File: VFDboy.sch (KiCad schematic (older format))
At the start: 44 parts, among them J1 AVR-ISP-6, SW1 RIGHT, SW2 A, SW3 DOWN, SW4 UP, SW5 LEFT, SW6 B, U1 ATmega32U4-MU, U2 SSD1306_VFD, U7 SRV05-4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

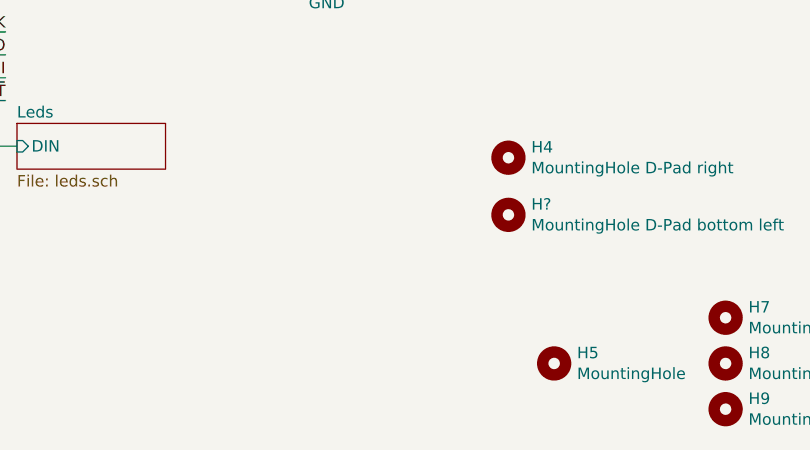
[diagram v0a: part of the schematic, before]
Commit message: Add Game Boy compatible D-Pad mounting holes
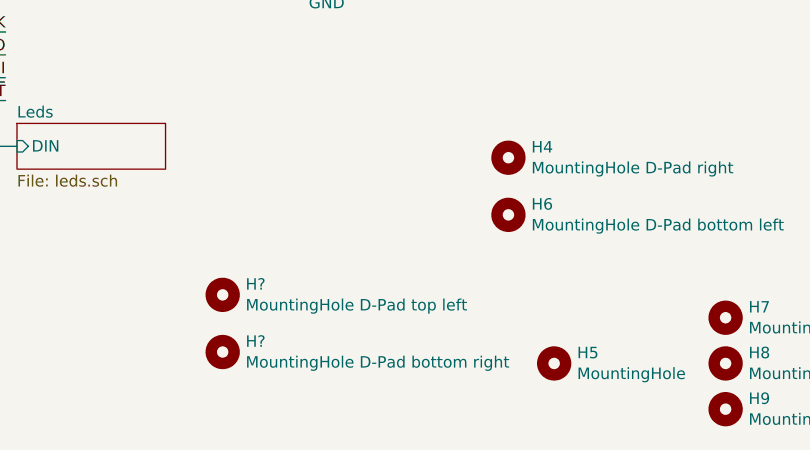
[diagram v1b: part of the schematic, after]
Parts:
- added H?: MountingHole D-Pad top left, MountingHole_GameBoy:MountingHole_GameBoy_DPAD, symbol Mechanical:MountingHole
- added H?: MountingHole D-Pad bottom right, MountingHole_GameBoy:MountingHole_GameBoy_DPAD, symbol Mechanical:MountingHole
- gave numbers to parts that had none: 1
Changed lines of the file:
@@
 $EndComp
 $Comp
-L Mechanical:MountingHole H?
+L Mechanical:MountingHole H6
 U 1 1 620E34B6
 P 4350 6700
-F 0 "H?" H 4450 6746 50  0000 L CNN
+F 0 "H6" H 4450 6746 50  0000 L CNN
 F 1 "MountingHole D-Pad bottom left" H 4450 6655 50  0000 L CNN
 F 2 "MountingHole_GBA:MountingHole_GBA_DPAD" H 4350 6700 50  0001 C CNN
@@
 	1    0    0    -1
 $EndComp
+$Comp
+L Mechanical:MountingHole H?
+U 1 1 620F5804
+P 3100 7050
+F 0 "H?" H 3200 7096 50  0000 L CNN
+F 1 "MountingHole D-Pad top left" H 3200 7005 50  0000 L CNN
+F 2 "MountingHole_GameBoy:MountingHole_GameBoy_DPAD" H 3100 7050 50  0001 C CNN
+F 3 "~" H 3100 7050 50  0001 C CNN
+	1    3100 7050
+	1    0    0    -1
+$EndComp
+$Comp
+L Mechanical:MountingHole H?
+U 1 1 621007C1
+P 3100 7300
+F 0 "H?" H 3200 7346 50  0000 L CNN
+F 1 "MountingHole D-Pad bottom right" H 3200 7255 50  0000 L CNN
+F 2 "MountingHole_GameBoy:MountingHole_GameBoy_DPAD" H 3100 7300 50  0001 C CNN
+F 3 "~" H 3100 7300 50  0001 C CNN
+	1    3100 7300
+	1    0    0    -1
+$EndComp

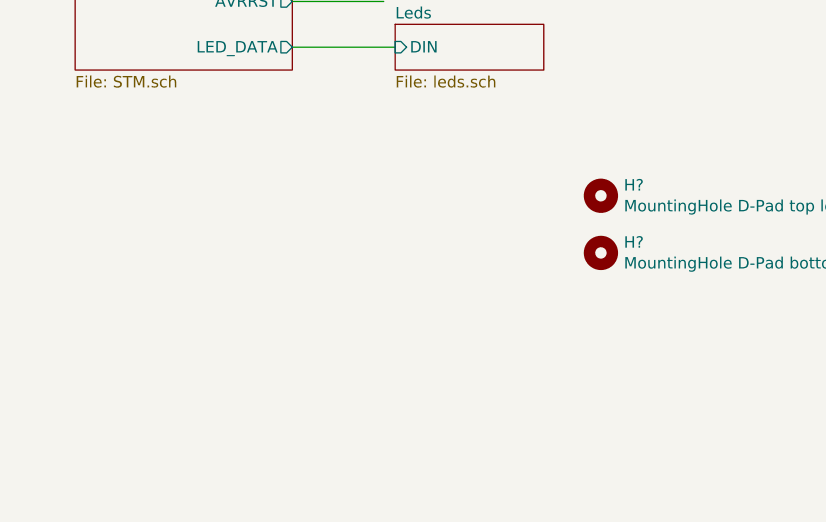
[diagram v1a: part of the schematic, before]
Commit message: Add AB button mounting
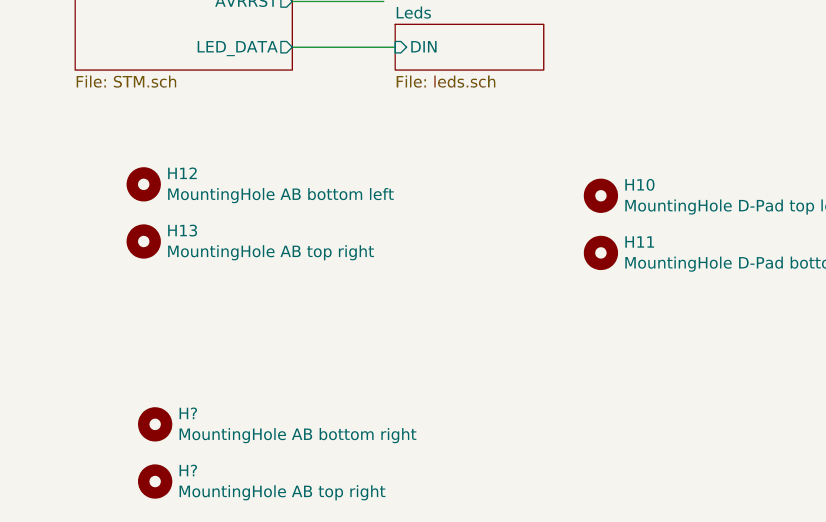
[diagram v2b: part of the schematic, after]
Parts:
- added H12: MountingHole AB bottom left, MountingHole_GameBoy:MountingHole_GameBoy_DPAD, symbol Mechanical:MountingHole
- added H13, H?: MountingHole AB top right, MountingHole_GameBoy:MountingHole_GameBoy_DPAD, symbol Mechanical:MountingHole
- added H?: MountingHole AB bottom right, MountingHole_GBA:MountingHole_GBA_AB_bottom_right, symbol Mechanical:MountingHole
- gave numbers to parts that had none: 2
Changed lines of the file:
@@
 $EndComp
 $Comp
-L Mechanical:MountingHole H?
+L Mechanical:MountingHole H10
 U 1 1 620F5804
 P 3100 7050
-F 0 "H?" H 3200 7096 50  0000 L CNN
+F 0 "H10" H 3200 7096 50  0000 L CNN
 F 1 "MountingHole D-Pad top left" H 3200 7005 50  0000 L CNN
 F 2 "MountingHole_GameBoy:MountingHole_GameBoy_DPAD" H 3100 7050 50  0001 C CNN
@@
 $EndComp
 $Comp
-L Mechanical:MountingHole H?
+L Mechanical:MountingHole H11
 U 1 1 621007C1
 P 3100 7300
-F 0 "H?" H 3200 7346 50  0000 L CNN
+F 0 "H11" H 3200 7346 50  0000 L CNN
 F 1 "MountingHole D-Pad bottom right" H 3200 7255 50  0000 L CNN
 F 2 "MountingHole_GameBoy:MountingHole_GameBoy_DPAD" H 3100 7300 50  0001 C CNN
@@
 	1    0    0    -1
 $EndComp
+$Comp
+L Mechanical:MountingHole H12
+U 1 1 6212859B
+P 1100 7000
+F 0 "H12" H 1200 7046 50  0000 L CNN
+F 1 "MountingHole AB bottom left" H 1200 6955 50  0000 L CNN
+F 2 "MountingHole_GameBoy:MountingHole_GameBoy_DPAD" H 1100 7000 50  0001 C CNN
+F 3 "~" H 1100 7000 50  0001 C CNN
+	1    1100 7000
+	1    0    0    -1
+$EndComp
+$Comp
+L Mechanical:MountingHole H13
+U 1 1 621285A1
+P 1100 7250
+F 0 "H13" H 1200 7296 50  0000 L CNN
+F 1 "MountingHole AB top right" H 1200 7205 50  0000 L CNN
+F 2 "MountingHole_GameBoy:MountingHole_GameBoy_DPAD" H 1100 7250 50  0001 C CNN
+F 3 "~" H 1100 7250 50  0001 C CNN
+	1    1100 7250
+	1    0    0    -1
+$EndComp
+$Comp
+L Mechanical:MountingHole H?
+U 1 1 6213C8C1
+P 1150 8050
+F 0 "H?" H 1250 8096 50  0000 L CNN
+F 1 "MountingHole AB bottom right" H 1250 8005 50  0000 L CNN
+F 2 "MountingHole_GBA:MountingHole_GBA_AB_bottom_right" H 1150 8050 50  0001 C CNN
+F 3 "~" H 1150 8050 50  0001 C CNN
+	1    1150 8050
+	1    0    0    -1
+$EndComp
+$Comp
+L Mechanical:MountingHole H?
+U 1 1 6213C8C7
+P 1150 8300
+F 0 "H?" H 1250 8346 50  0000 L CNN
+F 1 "MountingHole AB top right" H 1250 8255 50  0000 L CNN
+F 2 "MountingHole_GameBoy:MountingHole_GameBoy_DPAD" H 1150 8300 50  0001 C CNN
+F 3 "~" H 1150 8300 50  0001 C CNN
+	1    1150 8300
+	1    0    0    -1
+$EndComp

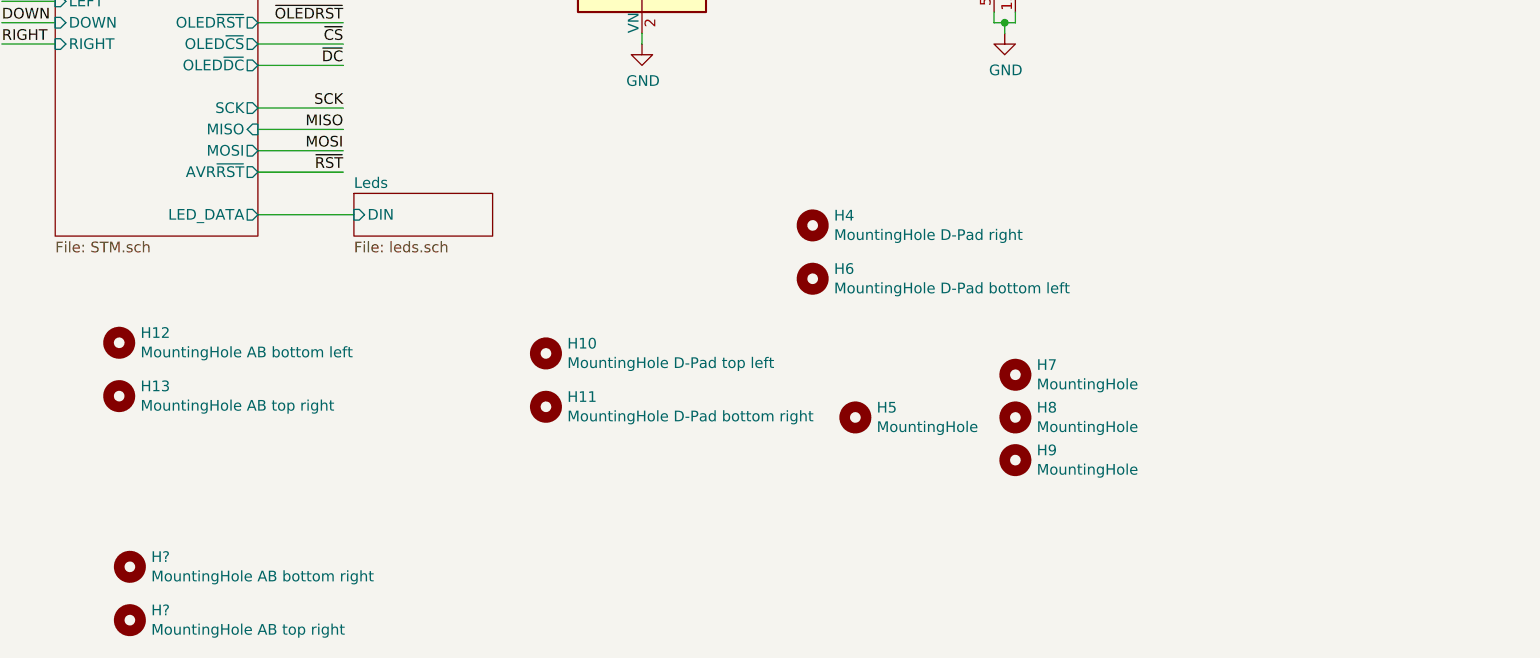
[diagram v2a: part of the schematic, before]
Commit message: Add tooling holes
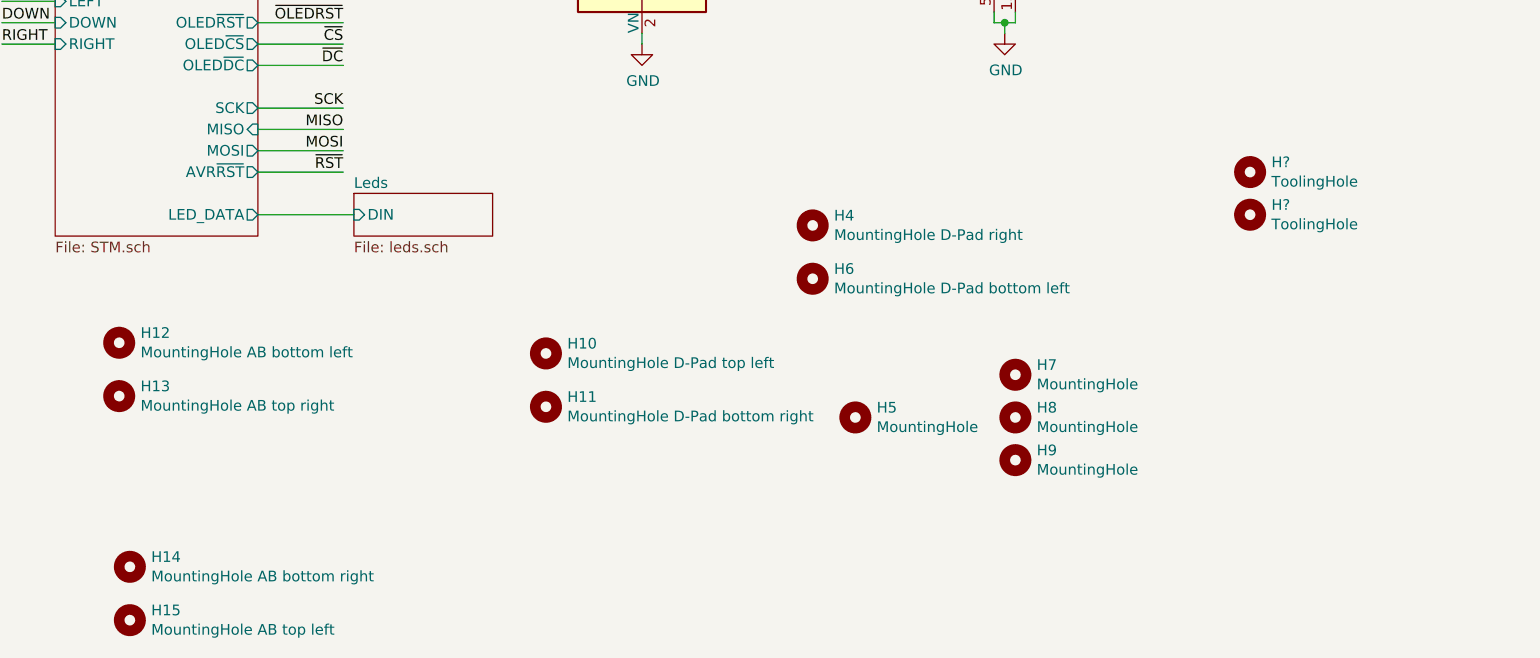
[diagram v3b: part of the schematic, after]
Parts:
- added H? (x2): ToolingHole, ToolingHole:ToolingHole_JLCSMT, symbol Mechanical:MountingHole
- H15: renamed from H?; value MountingHole AB top right -> MountingHole AB top left; footprint MountingHole_GameBoy:MountingHole_GameBoy_DPAD -> MountingHole:MountingHole_3.5mm
- gave numbers to parts that had none: 1
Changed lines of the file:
@@
 $EndComp
 $Comp
-L Mechanical:MountingHole H?
+L Mechanical:MountingHole H14
 U 1 1 6213C8C1
 P 1150 8050
-F 0 "H?" H 1250 8096 50  0000 L CNN
+F 0 "H14" H 1250 8096 50  0000 L CNN
 F 1 "MountingHole AB bottom right" H 1250 8005 50  0000 L CNN
 F 2 "MountingHole_GBA:MountingHole_GBA_AB_bottom_right" H 1150 8050 50  0001 C CNN
@@
 $EndComp
 $Comp
-L Mechanical:MountingHole H?
+L Mechanical:MountingHole H15
 U 1 1 6213C8C7
 P 1150 8300
-F 0 "H?" H 1250 8346 50  0000 L CNN
-F 1 "MountingHole AB top right" H 1250 8255 50  0000 L CNN
-F 2 "MountingHole_GameBoy:MountingHole_GameBoy_DPAD" H 1150 8300 50  0001 C CNN
+F 0 "H15" H 1250 8346 50  0000 L CNN
+F 1 "MountingHole AB top left" H 1250 8255 50  0000 L CNN
+F 2 "MountingHole:MountingHole_3.5mm" H 1150 8300 50  0001 C CNN
 F 3 "~" H 1150 8300 50  0001 C CNN
 	1    1150 8300
 	1    0    0    -1
 $EndComp
+$Comp
+L Mechanical:MountingHole H?
+U 1 1 621E7530
+P 6400 6200
+F 0 "H?" H 6500 6246 50  0000 L CNN
+F 1 "ToolingHole" H 6500 6155 50  0000 L CNN
+F 2 "ToolingHole:ToolingHole_JLCSMT" H 6400 6200 50  0001 C CNN
+F 3 "~" H 6400 6200 50  0001 C CNN
+	1    6400 6200
+	1    0    0    -1
+$EndComp
+$Comp
+L Mechanical:MountingHole H?
+U 1 1 621E8454
+P 6400 6400
+F 0 "H?" H 6500 6446 50  0000 L CNN
+F 1 "ToolingHole" H 6500 6355 50  0000 L CNN
+F 2 "ToolingHole:ToolingHole_JLCSMT" H 6400 6400 50  0001 C CNN
+F 3 "~" H 6400 6400 50  0001 C CNN
+	1    6400 6400
+	1    0    0    -1
+$EndComp

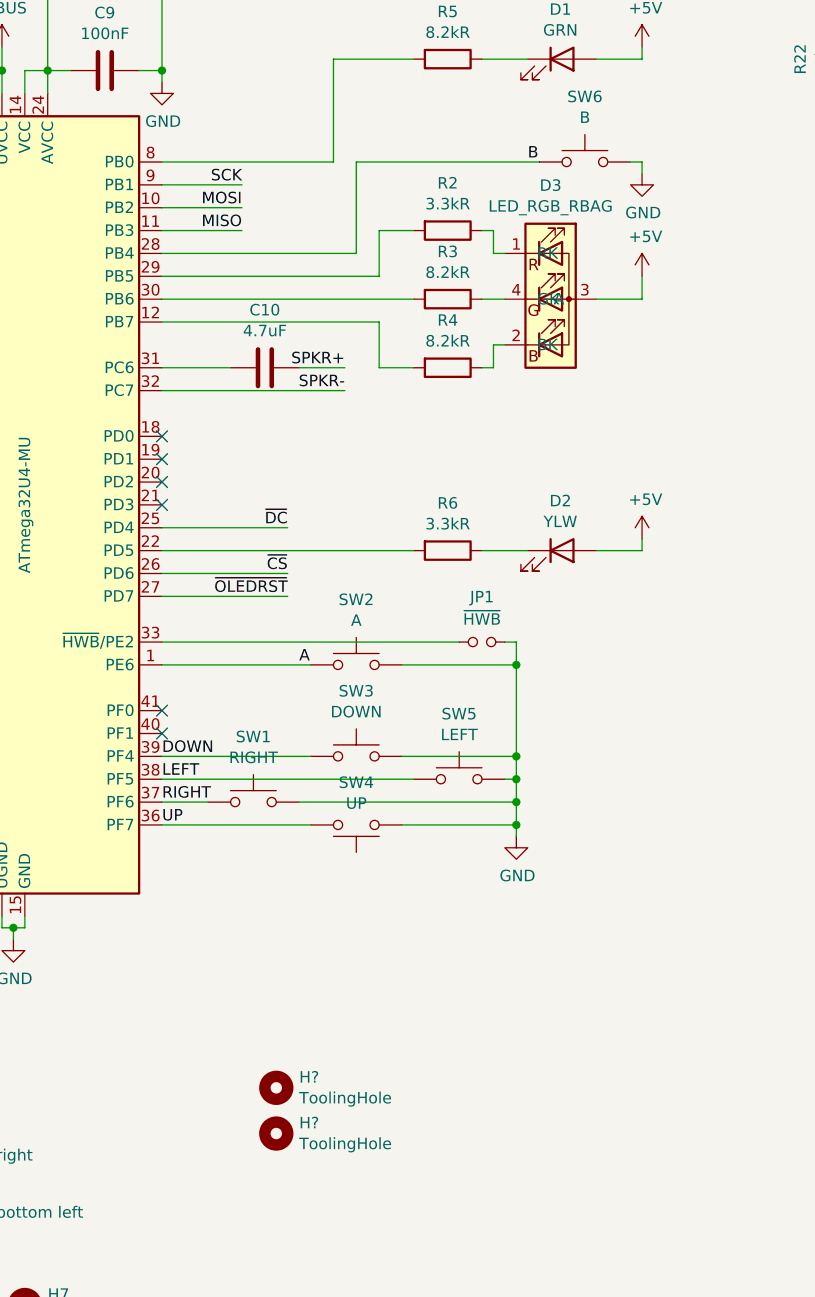
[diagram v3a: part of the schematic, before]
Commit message: Place and route WS2812 LEDs
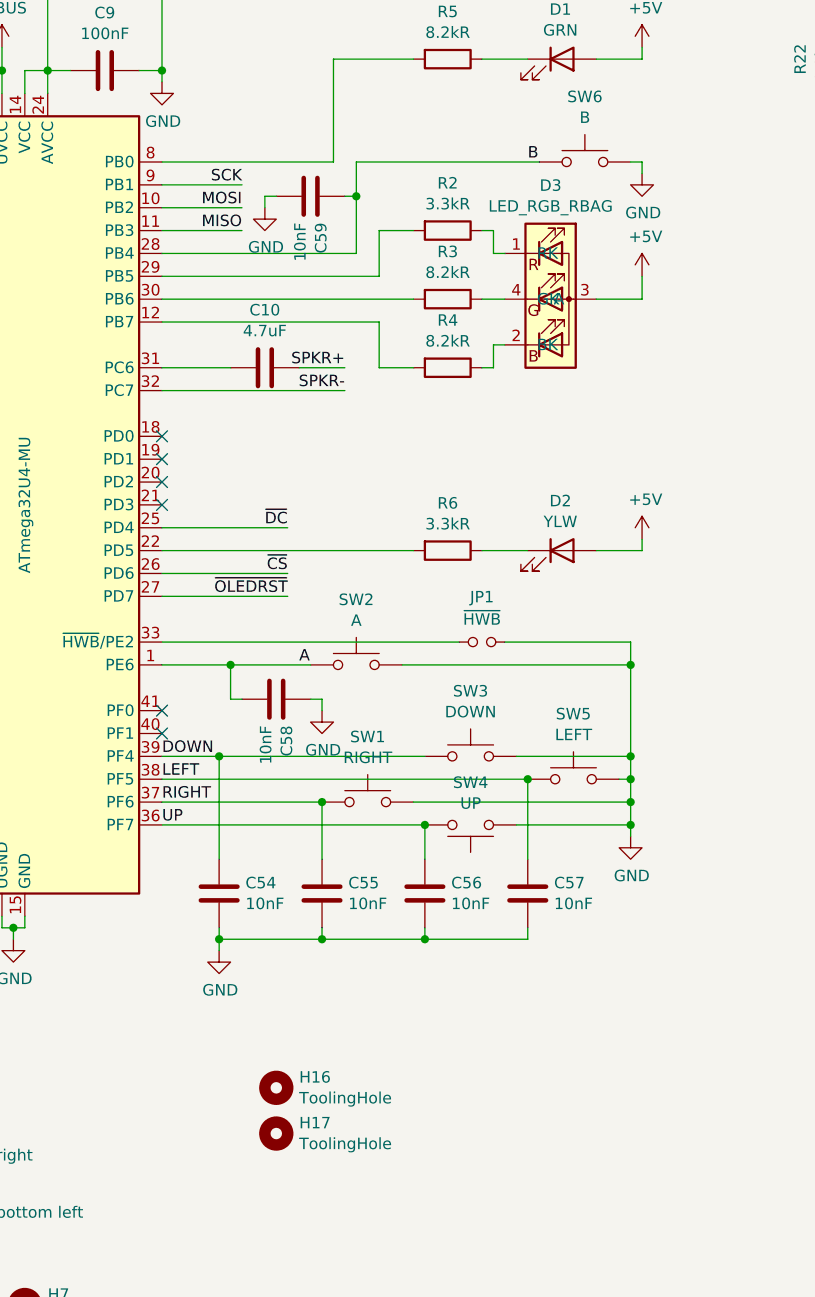
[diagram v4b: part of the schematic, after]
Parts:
- added C54, C55, C56, C57, C58, C59: 10nF, Capacitor_SMD:C_0402_1005Metric, symbol Device:C
- gave numbers to parts that had none: 2
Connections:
- net A: now also C58.2
- net B: now also C59.1
- net DOWN: now also C54.1
- net GND: now also C54.2, C55.2, C56.2, C57.2, C58.1, C59.2
- net LEFT: now also C57.1
- net RIGHT: now also C55.1
- net UP: now also C56.1
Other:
- moved on the sheet: SW1, SW3, SW4, SW5

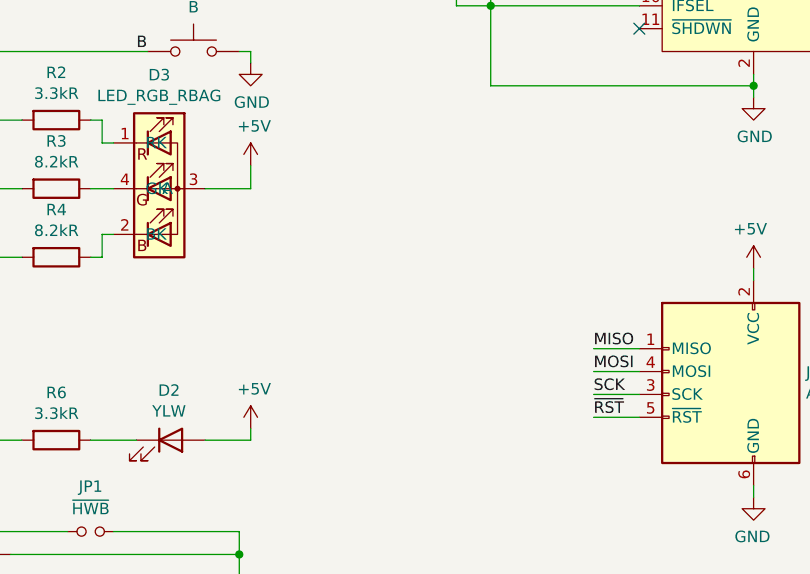
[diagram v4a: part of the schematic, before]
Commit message: Add option for elevated D-Pad
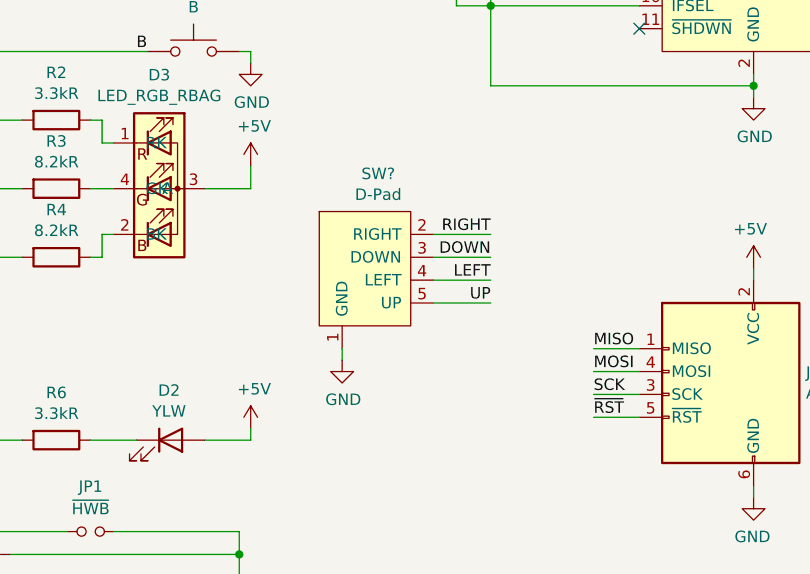
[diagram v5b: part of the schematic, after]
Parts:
- added SW?: D-Pad, button-daughterboard:Daughterboard_D-Pad, symbol Button_Daughterboard:D-Pad
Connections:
- net DOWN: now also SW?.3 (DOWN)
- net GND: now also SW?.1 (GND)
- net LEFT: now also SW?.4 (LEFT)
- net RIGHT: now also SW?.2 (RIGHT)
- net UP: now also SW?.5 (UP)
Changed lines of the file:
@@
 Wire Wire Line
 	6200 4350 5900 4350
+$Comp
+L Button_Daughterboard:D-Pad SW?
+U 1 1 623C0A73
+P 8500 3100
+F 0 "SW?" H 8558 3515 50  0000 C CNN
+F 1 "D-Pad" H 8558 3424 50  0000 C CNN
+F 2 "button-daughterboard:Daughterboard_D-Pad" H 8550 2950 50  0001 C CNN
+F 3 "" H 8550 2950 50  0001 C CNN
+	1    8500 3100
+	1    0    0    -1
+$EndComp
+$Comp
+L power:GND #PWR?
+U 1 1 623C143C
+P 8400 3500
+F 0 "#PWR?" H 8400 3250 50  0001 C CNN
+F 1 "GND" H 8405 3327 50  0000 C CNN
+F 2 "" H 8400 3500 50  0001 C CNN
+F 3 "" H 8400 3500 50  0001 C CNN
+	1    8400 3500
+	1    0    0    -1
+$EndComp
+Wire Wire Line
+	8400 3500 8400 3450
+Text Label 9050 2950 2    50   ~ 0
+RIGHT
+Wire Wire Line
+	9050 2950 8800 2950
+Text Label 9050 3050 2    50   ~ 0
+DOWN
+Wire Wire Line
+	9050 3050 8800 3050
+Text Label 9050 3150 2    50   ~ 0
+LEFT
+Wire Wire Line
+	9050 3150 8800 3150
+Text Label 9050 3250 2    50   ~ 0
+UP
+Wire Wire Line
+	9050 3250 8800 3250
 $EndSCHEMATC
